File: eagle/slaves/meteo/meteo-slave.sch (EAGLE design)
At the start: 37 parts, among them CON1 SPI, IC1 MCP1703CB, J2 RJ12RIGHTANGLE-I2C, J3 RJ12RIGHTANGLE-I2C, U1 ATMEGA328P_TQFP, X1 8MHz, X2 1503_09, X3 1503_09

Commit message: remove meteo capacitor for AREF
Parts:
- removed C1: 100nF, rcl:C-EUC0805K
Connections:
- removed net AREF: C1.1, U1.AREF
- net GND: no longer C1.2
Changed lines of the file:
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@@
-<attribute name="MPN" value="80-C1206C104K5R"/>
-</part>
-<part name="C1" library="rcl" library_urn="urn:adsk.eagle:library:334" deviceset="C-EU" device="C0805K" package3d_urn="urn:adsk.eagle:package:23681/2" value="100nF">
-<attribute name="ELECROW" value="C49678"/>
-<attribute name="LCSC" value="C49678"/>
 <attribute name="MPN" value="80-C1206C104K5R"/>
 </part>
@@
 <attribute name="LCSC" x="111.76" y="195.58" size="1.778" layer="96" display="off"/>
 </instance>
-<instance part="GND3" gate="1" x="96.52" y="114.3"/>
+<instance part="GND3" gate="1" x="106.68" y="114.3"/>
 <instance part="P+11" gate="G$1" x="106.68" y="147.32"/>
 <instance part="P+2" gate="G$1" x="129.54" y="134.62"/>
@@
 <attribute name="LCSC" x="114.3" y="137.16" size="1.778" layer="96" display="off"/>
 <attribute name="ELECROW" x="114.3" y="137.16" size="1.778" layer="96" display="off"/>
-</instance>
-<instance part="C1" gate="G$1" x="111.76" y="116.84" rot="R270">
-<attribute name="MPN" x="111.76" y="116.84" size="1.778" layer="96" rot="R270" display="off"/>
-<attribute name="LCSC" x="111.76" y="116.84" size="1.778" layer="96" rot="R270" display="off"/>
-<attribute name="ELECROW" x="111.76" y="116.84" size="1.778" layer="96" rot="R270" display="off"/>
 </instance>
 <instance part="C5" gate="G$1" x="121.92" y="78.74">
@@
 <pinref part="GND3" gate="1" pin="GND"/>
 <pinref part="S1" gate="G$1" pin="1"/>
-<pinref part="C1" gate="G$1" pin="2"/>
-<wire x1="96.52" y1="116.84" x2="106.68" y2="116.84" width="0.1524" layer="91"/>
 <wire x1="106.68" y1="116.84" x2="106.68" y2="119.38" width="0.1524" layer="91"/>
-<junction x="106.68" y="116.84"/>
 </segment>
 <segment>
@@
 </segment>
 </net>
-<net name="AREF" class="0">
-<segment>
-<wire x1="137.16" y1="116.84" x2="114.3" y2="116.84" width="0.1524" layer="91"/>
-<label x="121.92" y="116.84" size="1.778" layer="95"/>
-<pinref part="C1" gate="G$1" pin="1"/>
-<pinref part="U1" gate="U1" pin="AREF"/>
-</segment>
-</net>

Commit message: meteo-slave: add voltage monitoring of i2c
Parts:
- removed SJ1: A0, jumper:SJ
- added C11: 100nF, rcl:C-EUC0805K
- added R18: 1M, rcl:R-EU_R0805
- added R19: 100k, rcl:R-EU_R0805
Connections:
- net +5V: now also R18.2
- net A6: now also C11.2, R18.1, R19.2; no longer SJ1.1
- net GND: now also C11.1, R19.1; no longer SJ1.2
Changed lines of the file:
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@@
 <attribute name="MPN" value="621-1N5819HW-F"/>
 </part>
-<part name="SJ1" library="jumper" library_urn="urn:adsk.eagle:library:252" deviceset="SJ" device="" package3d_urn="urn:adsk.eagle:package:15471/1" value="A0"/>
 <part name="SJ2" library="jumper" library_urn="urn:adsk.eagle:library:252" deviceset="SJ" device="" package3d_urn="urn:adsk.eagle:package:15471/1" value="A1"/>
 <part name="GND13" library="SparkFun" deviceset="GND" device=""/>
@@
 <part name="X3" library="con-lumberg" deviceset="1503_09" device=""/>
 <part name="R7" library="rcl" deviceset="R-EU_" device="R0805" value="100"/>
+<part name="R18" library="rcl" deviceset="R-EU_" device="R0805" value="1M">
+<attribute name="ELECROW" value="C17514"/>
+<attribute name="LCSC" value="C17514"/>
+</part>
+<part name="R19" library="rcl" deviceset="R-EU_" device="R0805" value="100k">
+<attribute name="ELECROW" value="C17514"/>
+<attribute name="LCSC" value="C17514"/>
+</part>
+<part name="C11" library="rcl" library_urn="urn:adsk.eagle:library:334" deviceset="C-EU" device="C0805K" package3d_urn="urn:adsk.eagle:package:23681/2" value="100nF">
+<attribute name="ELECROW" value="C49678"/>
+<attribute name="LCSC" value="C49678"/>
+<attribute name="MPN" value="80-C1206C104K5R"/>
+</part>
+<part name="GND7" library="supply1" library_urn="urn:adsk.eagle:library:371" deviceset="GND" device=""/>
 </parts>
 <sheets>
@@
 <attribute name="LCSC" x="68.58" y="195.58" size="1.778" layer="96" display="off"/>
 </instance>
-<instance part="SJ1" gate="1" x="193.04" y="116.84" smashed="yes">
-<attribute name="NAME" x="190.5" y="119.38" size="1.778" layer="95"/>
-<attribute name="VALUE" x="191.77" y="117.348" size="1.778" layer="96"/>
-</instance>
 <instance part="SJ2" gate="1" x="193.04" y="114.3" smashed="yes">
 <attribute name="NAME" x="190.5" y="109.22" size="1.778" layer="95"/>
@@
 <instance part="X3" gate="G$1" x="276.86" y="33.02" rot="MR180"/>
 <instance part="R7" gate="G$1" x="271.78" y="43.18" rot="MR90"/>
+<instance part="R18" gate="G$1" x="261.62" y="162.56" rot="R90">
+<attribute name="LCSC" x="261.62" y="162.56" size="1.778" layer="96" rot="R90" display="off"/>
+<attribute name="ELECROW" x="261.62" y="162.56" size="1.778" layer="96" rot="R90" display="off"/>
+</instance>
+<instance part="R19" gate="G$1" x="261.62" y="149.86" rot="R90">
+<attribute name="LCSC" x="261.62" y="149.86" size="1.778" layer="96" rot="R90" display="off"/>
+<attribute name="ELECROW" x="261.62" y="149.86" size="1.778" layer="96" rot="R90" display="off"/>
+</instance>
+<instance part="C11" gate="G$1" x="256.54" y="149.86" rot="R180">
+<attribute name="MPN" x="256.54" y="149.86" size="1.778" layer="96" rot="R180" display="off"/>
+<attribute name="LCSC" x="256.54" y="149.86" size="1.778" layer="96" rot="R180" display="off"/>
+<attribute name="ELECROW" x="256.54" y="149.86" size="1.778" layer="96" rot="R180" display="off"/>
+</instance>
+<instance part="GND7" gate="1" x="256.54" y="142.24" smashed="yes">
+<attribute name="VALUE" x="254.635" y="140.335" size="1.27" layer="96"/>
+</instance>
 </instances>
 <busses>
@@
 </segment>
 <segment>
-<pinref part="SJ1" gate="1" pin="2"/>
 <pinref part="GND13" gate="1" pin="GND"/>
-<wire x1="198.12" y1="116.84" x2="203.2" y2="116.84" width="0.1524" layer="91"/>
-<wire x1="203.2" y1="116.84" x2="203.2" y2="114.3" width="0.1524" layer="91"/>
 <pinref part="SJ2" gate="1" pin="2"/>
 <wire x1="203.2" y1="114.3" x2="203.2" y2="111.76" width="0.1524" layer="91"/>
 <wire x1="198.12" y1="114.3" x2="203.2" y2="114.3" width="0.1524" layer="91"/>
-<junction x="203.2" y="114.3"/>
 </segment>
 <segment>
@@
 <pinref part="GND1" gate="1" pin="GND"/>
 <wire x1="266.7" y1="27.94" x2="271.78" y2="27.94" width="0.1524" layer="91"/>
+</segment>
+<segment>
+<wire x1="256.54" y1="144.78" x2="261.62" y2="144.78" width="0.1524" layer="91"/>
+<pinref part="R19" gate="G$1" pin="1"/>
+<pinref part="C11" gate="G$1" pin="1"/>
+<wire x1="256.54" y1="147.32" x2="256.54" y2="144.78" width="0.1524" layer="91"/>
+<junction x="256.54" y="144.78"/>
+<pinref part="GND7" gate="1" pin="GND"/>
 </segment>
 </net>
@@
 <net name="A6" class="0">
 <segment>
-<wire x1="180.34" y1="116.84" x2="187.96" y2="116.84" width="0.1524" layer="91"/>
+<wire x1="180.34" y1="116.84" x2="182.88" y2="116.84" width="0.1524" layer="91"/>
 <label x="182.88" y="116.84" size="1.27" layer="95"/>
 <pinref part="U1" gate="U1" pin="ADC6"/>
-<pinref part="SJ1" gate="1" pin="1"/>
+</segment>
+<segment>
+<pinref part="R18" gate="G$1" pin="1"/>
+<pinref part="R19" gate="G$1" pin="2"/>
+<wire x1="261.62" y1="157.48" x2="261.62" y2="154.94" width="0.1524" layer="91"/>
+<wire x1="261.62" y1="157.48" x2="266.7" y2="157.48" width="0.1524" layer="91"/>
+<label x="264.16" y="154.94" size="1.778" layer="95"/>
+<pinref part="C11" gate="G$1" pin="2"/>
+<wire x1="261.62" y1="157.48" x2="256.54" y2="157.48" width="0.1524" layer="91"/>
+<wire x1="256.54" y1="157.48" x2="256.54" y2="154.94" width="0.1524" layer="91"/>
+<junction x="261.62" y="157.48"/>
 </segment>
 </net>
@@
 <wire x1="66.04" y1="195.58" x2="53.34" y2="195.58" width="0.1524" layer="91"/>
 <label x="53.34" y="195.58" size="1.778" layer="95"/>
+</segment>
+<segment>
+<pinref part="R18" gate="G$1" pin="2"/>
+<wire x1="261.62" y1="170.18" x2="261.62" y2="167.64" width="0.1524" layer="91"/>
+<label x="261.62" y="170.18" size="1.778" layer="95"/>
 </segment>
 </net>
@@
 </nets>
 </sheet>
+<sheet>
+<plain>
+</plain>
+<instances>
+</instances>
+<busses>
+</busses>
+<nets>
+</nets>
+</sheet>

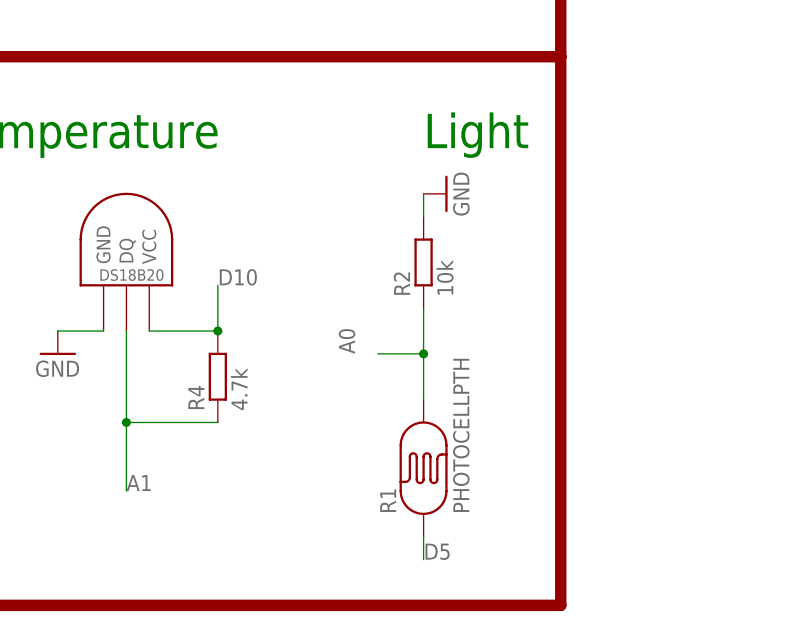
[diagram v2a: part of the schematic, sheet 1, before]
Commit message: meteo-slave: change light control to use internal pullup
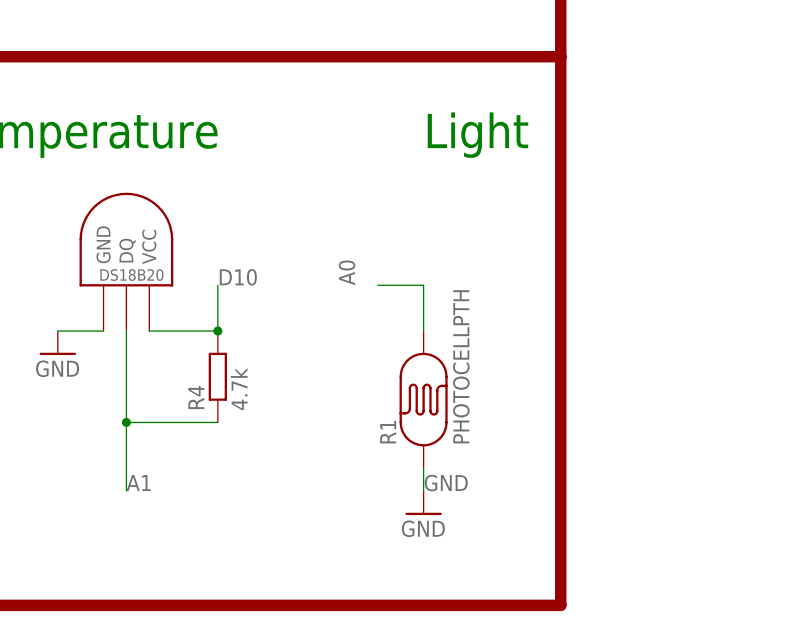
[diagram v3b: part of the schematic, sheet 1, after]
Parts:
- removed R2: 10k, resistor:R-EU_R0805
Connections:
- net A0: no longer R2.1
- net D5: no longer R1.P$1
- net GND: now also R1.P$1; no longer R2.2
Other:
- moved on the sheet: R1
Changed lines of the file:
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@@
 </part>
 <part name="R1" library="SparkFun" deviceset="PHOTOCELL" device="PTH"/>
-<part name="R2" library="resistor" library_urn="urn:adsk.eagle:library:348" deviceset="R-EU_" device="R0805" value="10k"/>
-<part name="GND2" library="supply1" library_urn="urn:adsk.eagle:library:371" deviceset="GND" device=""/>
 <part name="U$1" library="Ava" deviceset="DS1820" device="TO92"/>
 <part name="R4" library="resistor" library_urn="urn:adsk.eagle:library:348" deviceset="R-EU_" device="R0805" value="4.7k"/>
@@
 </part>
 <part name="GND7" library="supply1" library_urn="urn:adsk.eagle:library:371" deviceset="GND" device=""/>
+<part name="GND9" library="supply1" library_urn="urn:adsk.eagle:library:371" deviceset="GND" device=""/>
 </parts>
 <sheets>
@@
 <attribute name="LCSC" x="124.46" y="99.06" size="1.778" layer="96" rot="MR90" display="off"/>
 </instance>
-<instance part="R1" gate="G$1" x="193.04" y="15.24" rot="R90"/>
-<instance part="R2" gate="G$1" x="193.04" y="38.1" rot="R90"/>
-<instance part="GND2" gate="1" x="195.58" y="45.72" rot="R90"/>
+<instance part="R1" gate="G$1" x="193.04" y="22.86" rot="R90"/>
 <instance part="U$1" gate="G$1" x="160.02" y="35.56"/>
 <instance part="R4" gate="G$1" x="170.18" y="25.4" rot="R90"/>
@@
 <attribute name="VALUE" x="254.635" y="140.335" size="1.27" layer="96"/>
 </instance>
+<instance part="GND9" gate="1" x="193.04" y="10.16"/>
 </instances>
 <busses>
@@
 </segment>
 <segment>
-<pinref part="R2" gate="G$1" pin="2"/>
-<pinref part="GND2" gate="1" pin="GND"/>
-<wire x1="193.04" y1="45.72" x2="193.04" y2="43.18" width="0.1524" layer="91"/>
-</segment>
-<segment>
 <pinref part="U$1" gate="G$1" pin="GND"/>
 <pinref part="GND4" gate="1" pin="GND"/>
@@
 <junction x="256.54" y="144.78"/>
 <pinref part="GND7" gate="1" pin="GND"/>
+</segment>
+<segment>
+<pinref part="R1" gate="G$1" pin="P$1"/>
+<wire x1="193.04" y1="12.7" x2="193.04" y2="15.24" width="0.1524" layer="91"/>
+<label x="193.04" y="12.7" size="1.778" layer="95"/>
+<pinref part="GND9" gate="1" pin="GND"/>
 </segment>
 </net>
@@
 <segment>
 <pinref part="R1" gate="G$1" pin="P$2"/>
-<pinref part="R2" gate="G$1" pin="1"/>
-<wire x1="193.04" y1="22.86" x2="193.04" y2="27.94" width="0.1524" layer="91"/>
-<wire x1="193.04" y1="27.94" x2="193.04" y2="33.02" width="0.1524" layer="91"/>
-<wire x1="187.96" y1="27.94" x2="193.04" y2="27.94" width="0.1524" layer="91"/>
-<junction x="193.04" y="27.94"/>
-<label x="185.42" y="27.94" size="1.778" layer="95" rot="R90"/>
+<wire x1="193.04" y1="30.48" x2="193.04" y2="35.56" width="0.1524" layer="91"/>
+<wire x1="187.96" y1="35.56" x2="193.04" y2="35.56" width="0.1524" layer="91"/>
+<label x="185.42" y="35.56" size="1.778" layer="95" rot="R90"/>
 </segment>
 </net>
@@
 <pinref part="U1" gate="U1" pin="PD5(T1)"/>
 </segment>
-<segment>
-<pinref part="R1" gate="G$1" pin="P$1"/>
-<wire x1="193.04" y1="5.08" x2="193.04" y2="7.62" width="0.1524" layer="91"/>
-<label x="193.04" y="5.08" size="1.778" layer="95"/>
-</segment>
-</net>
+</net>
